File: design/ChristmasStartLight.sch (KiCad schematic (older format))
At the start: 9 parts, among them P1 CONN_2, Q1 MPS2222A, U1 TCL555CP

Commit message: Parts and PCB done
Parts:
- added SW1: MHSS1104, symbol SPDT
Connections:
- no-connect marks 2 -> 3
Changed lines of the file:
@@
 LIBS:bth-transistor
 LIBS:bth-ic
+LIBS:bth-switch
 LIBS:ChristmasStartLight-cache
 EELAYER 24 0
@@
 L VCC #PWR03
 U 1 1 522FBE7A
-P 4450 2800
-F 0 "#PWR03" H 4450 2900 30  0001 C CNN
-F 1 "VCC" H 4450 2900 30  0000 C CNN
-F 2 "" H 4450 2800 60  0000 C CNN
-F 3 "" H 4450 2800 60  0000 C CNN
-	1    4450 2800
+P 5400 2700
+F 0 "#PWR03" H 5400 2800 30  0001 C CNN
+F 1 "VCC" H 5400 2800 30  0000 C CNN
+F 2 "" H 5400 2700 60  0000 C CNN
+F 3 "" H 5400 2700 60  0000 C CNN
+	1    5400 2700
 	0    1    1    0
 $EndComp
@@
 	2900 4450 2900 4175
 Connection ~ 2900 4175
+$Comp
+L SPDT SW1
+U 1 1 523530BD
+P 4950 2800
+F 0 "SW1" H 4850 2900 70  0000 C CNN
+F 1 "MHSS1104" H 4950 2600 70  0000 C CNN
+F 2 "" H 4950 2800 60  0000 C CNN
+F 3 "" H 4950 2800 60  0000 C CNN
+	1    4950 2800
+	1    0    0    -1
+$EndComp
+NoConn ~ 5400 2900
 $EndSCHEMATC

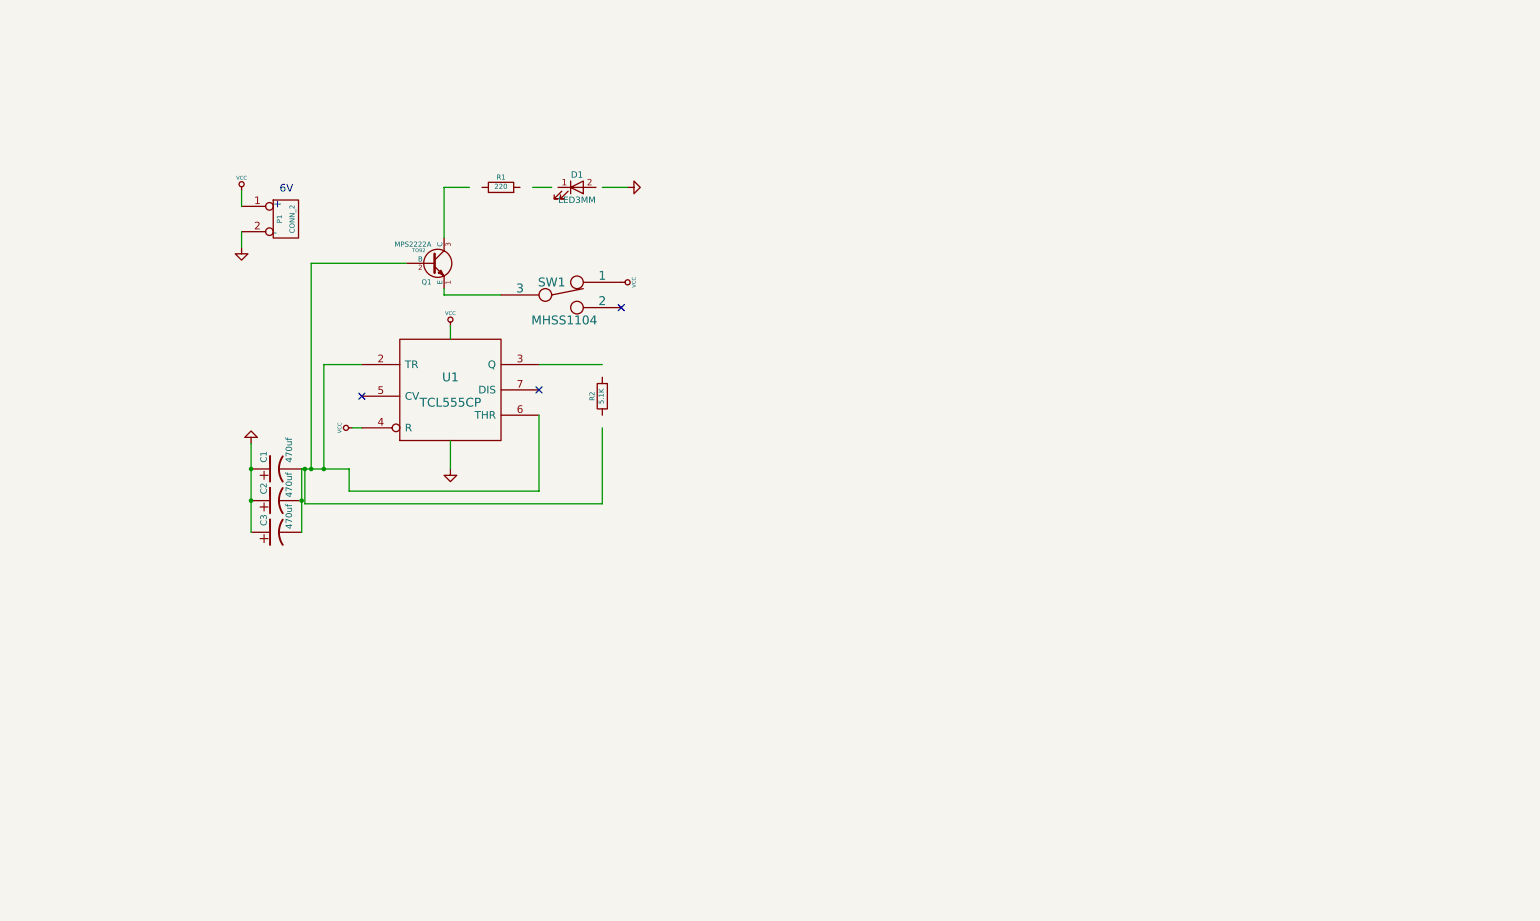
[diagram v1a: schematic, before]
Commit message: first smd version v2
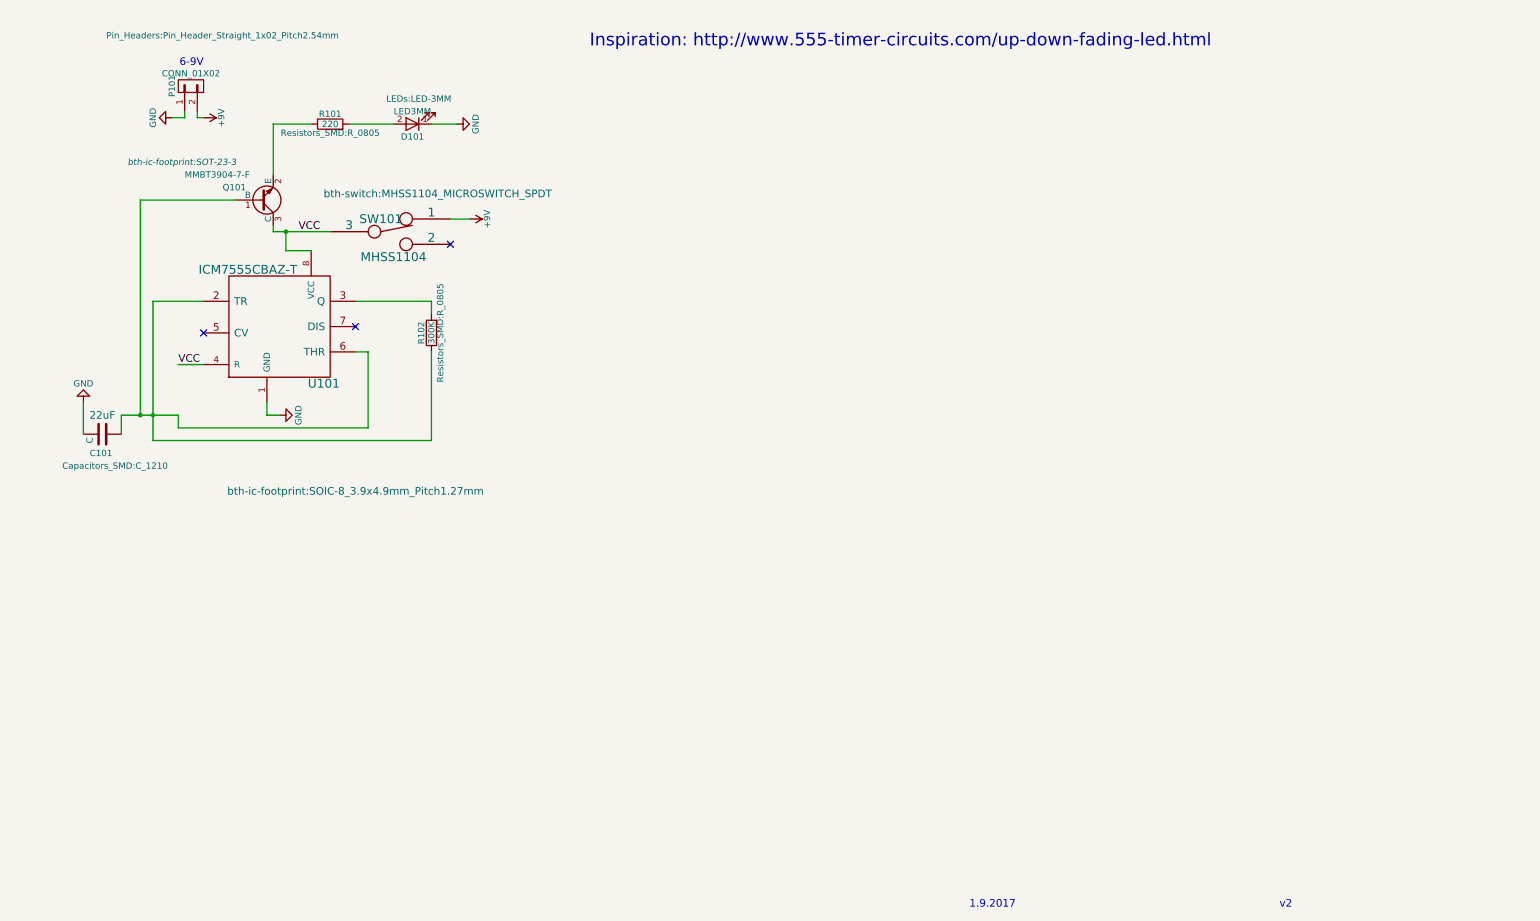
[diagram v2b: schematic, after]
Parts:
- removed C1, C2, C3: 470uf, symbol CP1
- removed D1: LED3MM, symbol LED
- removed P1: CONN_2, symbol CONN_2
- removed Q1: MPS2222A, TO92, symbol MPS2222A
- removed R1: 220, symbol R
- removed R2: 5.1K, symbol R
- removed SW1: MHSS1104, symbol SPDT
- removed U1: TCL555CP, symbol TCL555CP
- added C101: C, Capacitors_SMD:C_1210, symbol C
- added D101: LED3MM, LEDs:LED-3MM, symbol LED
- added P101: CONN_01X02, Pin_Headers:Pin_Header_Straight_1x02_Pitch2.54mm, symbol CONN_01X02
- added Q101: MMBT3904-7-F, bth-ic-footprint:SOT-23-3, symbol MMBT3904-7-F
- added R101: 220, Resistors_SMD:R_0805, symbol R
- added R102: 300K, Resistors_SMD:R_0805, symbol R
- added SW101: MHSS1104, bth-switch:MHSS1104_MICROSWITCH_SPDT, symbol SPDT
- added U101: ICM7555CBAZ-T, bth-ic-footprint:SOIC-8_3.9x4.9mm_Pitch1.27mm, symbol ICM7555CBAZ-T
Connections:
- net labels added: +9V
- wire segments 25 -> 31
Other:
- note added: "1.9.2017"
- note added: "6-9V"
- note added: "Inspiration: http://www.555-timer-circuits.com/up-down-fading-led.html"
- note added: "v2"
- note removed: "+"
- note removed: "-"
- note removed: "6V"

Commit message: Started on v3 of the schematic.  Still need to do PCB layout.
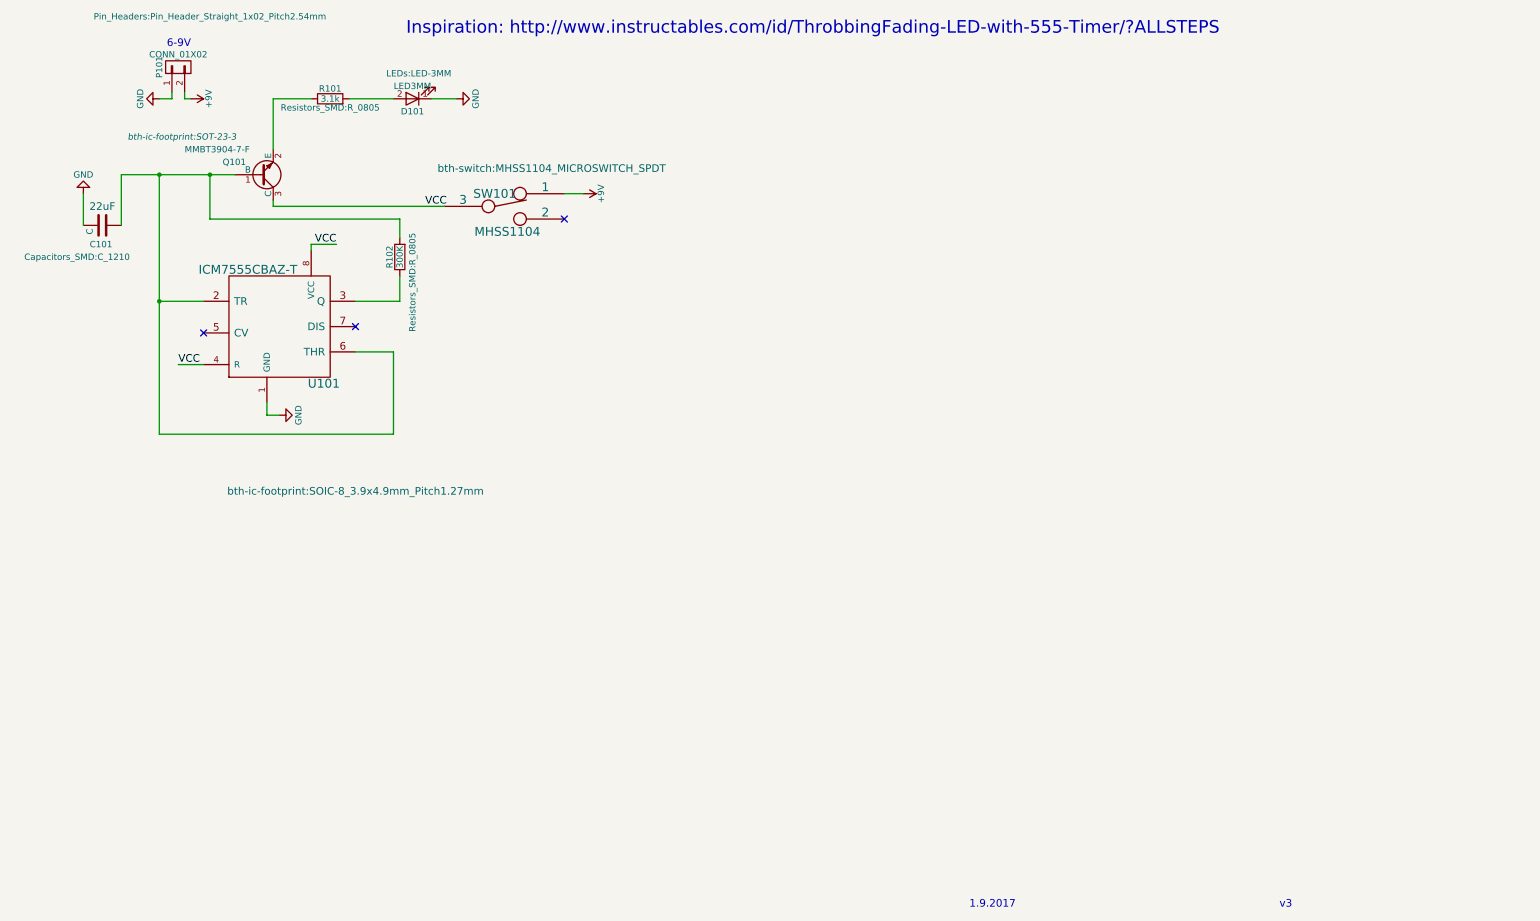
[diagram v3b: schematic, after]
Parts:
- R101: value 220 -> 3.1k
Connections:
- net at C101.1, Q101.1 (B), U101.2 (TR)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: now also R102.2; no longer R102.1
- net at U101.3 (Q): now also R102.1; no longer R102.2
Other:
- note added: "Inspiration: http://www.instructables.com/id/ThrobbingFading-LED-with-555-Timer/?ALLSTEPS"
- note added: "v3"
- note removed: "Inspiration: http://www.555-timer-circuits.com/up-down-fading-led.html"
- note removed: "v2"
- moved on the sheet: C101, D101, P101, Q101, R101, R102, SW101
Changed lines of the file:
@@
 $EndDescr
 NoConn ~ 3300 3050
-Text Notes 2100 1000 2    60   ~ 0
+Text Notes 2000 850  2    60   ~ 0
 6-9V
 NoConn ~ 2100 3100
@@
 L SPDT SW101
 U 1 1 5872F9EC
-P 3600 2300
-F 0 "SW101" H 3500 2400 70  0000 C CNN
-F 1 "MHSS1104" H 3600 2100 70  0000 C CNN
-F 2 "bth-switch:MHSS1104_MICROSWITCH_SPDT" H 3950 2600 60  0000 C CNN
-F 3 "" H 3600 2300 60  0000 C CNN
-	1    3600 2300
+P 4500 2100
+F 0 "SW101" H 4400 2200 70  0000 C CNN
+F 1 "MHSS1104" H 4500 1900 70  0000 C CNN
+F 2 "bth-switch:MHSS1104_MICROSWITCH_SPDT" H 4850 2400 60  0000 C CNN
+F 3 "" H 4500 2100 60  0000 C CNN
+	1    4500 2100
 	1    0    0    -1
 $EndComp
-NoConn ~ 4050 2400
-$Comp
-L GND #PWR101
+NoConn ~ 4950 2200
+$Comp
+L GND #PWR01
 U 1 1 5872FD24
-P 1150 3650
-F 0 "#PWR101" H 1150 3400 50  0001 C CNN
-F 1 "GND" H 1150 3500 50  0000 C CNN
-F 2 "" H 1150 3650 50  0000 C CNN
-F 3 "" H 1150 3650 50  0000 C CNN
-	1    1150 3650
+P 1150 2000
+F 0 "#PWR01" H 1150 1750 50  0001 C CNN
+F 1 "GND" H 1150 1850 50  0000 C CNN
+F 2 "" H 1150 2000 50  0000 C CNN
+F 3 "" H 1150 2000 50  0000 C CNN
+	1    1150 2000
 	-1   0    0    1
 $EndComp
@@
 L LED D101
 U 1 1 58730AEF
-P 3750 1450
-F 0 "D101" H 3750 1550 50  0000 C CNN
-F 1 "LED3MM" H 3750 1350 50  0000 C CNN
-F 2 "LEDs:LED-3MM" H 3700 1250 50  0000 C CNN
-F 3 "" H 3750 1450 50  0000 C CNN
-	1    3750 1450
+P 3750 1250
+F 0 "D101" H 3750 1350 50  0000 C CNN
+F 1 "LED3MM" H 3750 1150 50  0000 C CNN
+F 2 "LEDs:LED-3MM" H 3700 1050 50  0000 C CNN
+F 3 "" H 3750 1250 50  0000 C CNN
+	1    3750 1250
 	-1   0    0    1
 $EndComp
@@
 L R R101
 U 1 1 58730C5A
-P 3100 1450
-F 0 "R101" V 3180 1450 50  0000 C CNN
-F 1 "220" V 3100 1450 50  0000 C CNN
-F 2 "Resistors_SMD:R_0805" V 3030 1450 50  0000 C CNN
-F 3 "" H 3100 1450 50  0000 C CNN
-	1    3100 1450
-	0    -1   -1   0
-$EndComp
-$Comp
-L GND #PWR102
+P 3100 1250
+F 0 "R101" V 3180 1250 50  0000 C CNN
+F 1 "3.1k" V 3100 1250 50  0000 C CNN
+F 2 "Resistors_SMD:R_0805" V 3030 1250 50  0000 C CNN
+F 3 "" H 3100 1250 50  0000 C CNN
+	1    3100 1250
+	0    -1   -1   0
+$EndComp
+$Comp
+L GND #PWR02
 U 1 1 58731498
-P 1850 1400
-F 0 "#PWR102" H 1850 1150 50  0001 C CNN
-F 1 "GND" H 1850 1250 50  0000 C CNN
-F 2 "" H 1850 1400 50  0000 C CNN
-F 3 "" H 1850 1400 50  0000 C CNN
-	1    1850 1400
+P 1750 1250
+F 0 "#PWR02" H 1750 1000 50  0001 C CNN
+F 1 "GND" H 1750 1100 50  0000 C CNN
+F 2 "" H 1750 1250 50  0000 C CNN
+F 3 "" H 1750 1250 50  0000 C CNN
+	1    1750 1250
 	0    1    -1   0
 $EndComp
@@
 L R R102
 U 1 1 58731A55
-P 3900 3100
-F 0 "R102" V 3980 3100 50  0000 C CNN
-F 1 "300K" V 3900 3100 50  0000 C CNN
-F 2 "Resistors_SMD:R_0805" V 3830 3100 50  0000 C CNN
-F 3 "" H 3900 3100 50  0000 C CNN
-	1    3900 3100
+P 3650 2500
+F 0 "R102" V 3730 2500 50  0000 C CNN
+F 1 "300K" V 3650 2500 50  0000 C CNN
+F 2 "Resistors_SMD:R_0805" V 3550 2700 50  0000 C CNN
+F 3 "" H 3650 2500 50  0000 C CNN
+	1    3650 2500
 	-1   0    0    1
 $EndComp
 Wire Wire Line
-	2650 2250 2650 2300
-Wire Wire Line
-	2650 2300 3100 2300
-Wire Wire Line
-	2650 1850 2650 1450
-Wire Wire Line
-	2650 1450 2950 1450
-Wire Wire Line
-	3250 1450 3600 1450
-Wire Wire Line
-	3900 1450 4100 1450
-Wire Wire Line
-	3300 2850 3900 2850
-Wire Wire Line
-	1900 3850 3400 3850
-Wire Wire Line
-	3400 3850 3400 3250
-Wire Wire Line
-	1700 2850 2100 2850
-Wire Wire Line
-	1600 2050 2350 2050
-Wire Wire Line
-	3900 3250 3900 3950
-Wire Wire Line
-	3900 3950 1700 3950
-Wire Wire Line
-	1700 3950 1700 2850
-Wire Wire Line
-	1900 3750 1900 3850
-Wire Wire Line
-	1450 3750 1900 3750
-Connection ~ 1700 3750
-Wire Wire Line
-	1600 2050 1600 3750
-Connection ~ 1600 3750
-Wire Wire Line
-	4200 2200 4050 2200
-Wire Wire Line
-	3900 2850 3900 2950
-$Comp
-L GND #PWR104
+	2650 1650 2650 1250
+Wire Wire Line
+	2650 1250 2950 1250
+Wire Wire Line
+	3250 1250 3600 1250
+Wire Wire Line
+	3900 1250 4100 1250
+Wire Wire Line
+	1450 1850 2350 1850
+Wire Wire Line
+	5100 2000 4950 2000
+$Comp
+L GND #PWR03
 U 1 1 5873274C
 P 2700 3750
-F 0 "#PWR104" H 2700 3500 50  0001 C CNN
+F 0 "#PWR03" H 2700 3500 50  0001 C CNN
 F 1 "GND" H 2700 3600 50  0000 C CNN
 F 2 "" H 2700 3750 50  0000 C CNN
@@
 Wire Wire Line
 	2600 3750 2600 3650
-Text Notes 5150 850  0    100  ~ 0
-Inspiration: http://www.555-timer-circuits.com/up-down-fading-led.html
-Wire Wire Line
-	1450 3900 1450 3750
-Wire Wire Line
-	1150 3900 1150 3650
+Text Notes 3700 750  0    100  ~ 0
+Inspiration: http://www.instructables.com/id/ThrobbingFading-LED-with-555-Timer/?ALLSTEPS
+Wire Wire Line
+	1450 1850 1450 2250
+Wire Wire Line
+	1150 2250 1150 2000
 $Comp
 L ICM7555CBAZ-T U101
@@
 	1    0    0    -1
 $EndComp
-Wire Wire Line
-	3400 3250 3300 3250
-Text Label 2850 2300 0    60   ~ 0
+Text Label 3850 2100 0    60   ~ 0
 VCC
 $Comp
-L +9V #PWR106
+L +9V #PWR04
 U 1 1 58733410
-P 4200 2200
-F 0 "#PWR106" H 4200 2050 50  0001 C CNN
-F 1 "+9V" H 4200 2340 50  0000 C CNN
-F 2 "" H 4200 2200 50  0000 C CNN
-F 3 "" H 4200 2200 50  0000 C CNN
-	1    4200 2200
+P 5100 2000
+F 0 "#PWR04" H 5100 1850 50  0001 C CNN
+F 1 "+9V" H 5100 2140 50  0000 C CNN
+F 2 "" H 5100 2000 50  0000 C CNN
+F 3 "" H 5100 2000 50  0000 C CNN
+	1    5100 2000
 	0    1    1    0
 $EndComp
 $Comp
-L +9V #PWR103
+L +9V #PWR05
 U 1 1 58733487
-P 2100 1400
-F 0 "#PWR103" H 2100 1250 50  0001 C CNN
-F 1 "+9V" H 2100 1540 50  0000 C CNN
-F 2 "" H 2100 1400 50  0000 C CNN
-F 3 "" H 2100 1400 50  0000 C CNN
-	1    2100 1400
+P 2000 1250
+F 0 "#PWR05" H 2000 1100 50  0001 C CNN
+F 1 "+9V" H 2000 1390 50  0000 C CNN
+F 2 "" H 2000 1250 50  0000 C CNN
+F 3 "" H 2000 1250 50  0000 C CNN
+	1    2000 1250
 	0    1    1    0
 $EndComp
 Wire Wire Line
-	2950 2450 2750 2450
+	2950 2450 2950 2450
 Wire Wire Line
 	2100 3350 1900 3350
 Text Label 1900 3350 0    60   ~ 0
 VCC
-Wire Wire Line
-	2750 2450 2750 2300
-Connection ~ 2750 2300
-$Comp
-L GND #PWR105
+$Comp
+L GND #PWR06
 U 1 1 58733BE9
-P 4100 1450
-F 0 "#PWR105" H 4100 1200 50  0001 C CNN
-F 1 "GND" H 4100 1300 50  0000 C CNN
-F 2 "" H 4100 1450 50  0000 C CNN
-F 3 "" H 4100 1450 50  0000 C CNN
-	1    4100 1450
+P 4100 1250
+F 0 "#PWR06" H 4100 1000 50  0001 C CNN
+F 1 "GND" H 4100 1100 50  0000 C CNN
+F 2 "" H 4100 1250 50  0000 C CNN
+F 3 "" H 4100 1250 50  0000 C CNN
+	1    4100 1250
 	0    -1   -1   0
 $EndComp
@@
 L CONN_01X02 P101
 U 1 1 58743BAC
-P 2000 1150
-F 0 "P101" H 2000 1300 50  0000 C CNN
-F 1 "CONN_01X02" V 2100 1150 50  0000 C CNN
-F 2 "Pin_Headers:Pin_Header_Straight_1x02_Pitch2.54mm" V 2400 900 50  0000 C CNN
-F 3 "" H 2000 1150 50  0000 C CNN
-	1    2000 1150
-	0    -1   -1   0
-$EndComp
-Wire Wire Line
-	1850 1400 1950 1400
-Wire Wire Line
-	1950 1400 1950 1350
-Wire Wire Line
-	2050 1350 2050 1400
-Wire Wire Line
-	2050 1400 2100 1400
+P 1900 1000
+F 0 "P101" H 1900 1150 50  0000 C CNN
+F 1 "CONN_01X02" V 2000 1000 50  0000 C CNN
+F 2 "Pin_Headers:Pin_Header_Straight_1x02_Pitch2.54mm" V 2300 750 50  0000 C CNN
+F 3 "" H 1900 1000 50  0000 C CNN
+	1    1900 1000
+	0    -1   -1   0
+$EndComp
+Wire Wire Line
+	1750 1250 1850 1250
+Wire Wire Line
+	1850 1250 1850 1200
+Wire Wire Line
+	1950 1200 1950 1250
+Wire Wire Line
+	1950 1250 2000 1250
 Text Notes 8150 7650 0    60   ~ 0
 1.9.2017
 Text Notes 10600 7650 0    60   ~ 0
-v2
+v3
 $Comp
 L MMBT3904-7-F Q101
 U 1 1 587587C0
-P 2550 2050
-F 0 "Q101" H 2250 1950 50  0000 L CNN
-F 1 "MMBT3904-7-F" H 1950 1850 50  0000 L CNN
-F 2 "bth-ic-footprint:SOT-23-3" H 1500 1750 50  0000 L CIN
-F 3 "" H 2550 2050 50  0000 L CNN
-	1    2550 2050
+P 2550 1850
+F 0 "Q101" H 2250 1750 50  0000 L CNN
+F 1 "MMBT3904-7-F" H 1950 1650 50  0000 L CNN
+F 2 "bth-ic-footprint:SOT-23-3" H 1500 1550 50  0000 L CIN
+F 3 "" H 2550 1850 50  0000 L CNN
+	1    2550 1850
 	1    0    0    1
 $EndComp
@@
 L C C101
 U 1 1 58759A84
-P 1300 3900
-F 0 "C101" V 1450 3800 50  0000 L CNN
-F 1 "C" H 1325 3800 50  0000 L CNN
-F 2 "Capacitors_SMD:C_1210" V 1550 4000 50  0000 C CNN
-F 3 "" H 1300 3900 50  0000 C CNN
-F 4 "22uF" V 1150 3900 60  0000 C CNN "Specification"
-	1    1300 3900
+P 1300 2250
+F 0 "C101" V 1450 2150 50  0000 L CNN
+F 1 "C" H 1325 2150 50  0000 L CNN
+F 2 "Capacitors_SMD:C_1210" V 1550 2050 50  0000 C CNN
+F 3 "" H 1300 2250 50  0000 C CNN
+F 4 "22uF" V 1150 2250 60  0000 C CNN "Specification"
+	1    1300 2250
 	0    1    1    0
 $EndComp
+Wire Wire Line
+	2650 2100 4000 2100
+Wire Wire Line
+	3300 3250 3600 3250
+Wire Wire Line
+	1750 2850 2100 2850
+Wire Wire Line
+	3600 3250 3600 3900
+Wire Wire Line
+	3600 3900 1750 3900
+Wire Wire Line
+	1750 3900 1750 1850
+Connection ~ 1750 2850
+Wire Wire Line
+	2950 2450 2950 2400
+Wire Wire Line
+	2950 2400 3150 2400
+Text Label 3150 2400 2    60   ~ 0
+VCC
+Wire Wire Line
+	3300 2850 3650 2850
+Wire Wire Line
+	3650 2850 3650 2650
+Wire Wire Line
+	2150 1850 2150 2200
+Wire Wire Line
+	2150 2200 3650 2200
+Wire Wire Line
+	3650 2200 3650 2350
+Connection ~ 2150 1850
+Connection ~ 1750 1850
+Wire Wire Line
+	2650 2050 2650 2100
 $EndSCHEMATC

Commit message: Misc changes
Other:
- note added: "1.24.2017"
- note removed: "1.9.2017"
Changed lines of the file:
@@
 	1950 1250 2000 1250
 Text Notes 8150 7650 0    60   ~ 0
-1.9.2017
+1.24.2017
 Text Notes 10600 7650 0    60   ~ 0
 v3
